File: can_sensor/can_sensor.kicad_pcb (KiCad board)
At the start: 2 copper layers, 53.3 x 25.4 mm, 54 parts, among them P1 IO1, P2 IO2, P4 CONN_01X03, P5 USB, P6 CAN_IN, P7 CAN_OUT, SW1 RESET, SW2 BOOT, U1 NJM2870F0, U2 MIC5317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

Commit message: Fixed boot button going to boot1 instead of boot0
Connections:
- P1 pad 0: GND -> (no net)
- P2 pad 0: GND -> (no net)
- P6 pad 0: GND -> (no net)
- P7 pad 0: GND -> (no net)
- U3 pad 1: Net-(U3-Pad1) -> (no net)
- U3 pad 10: Net-(U3-Pad10) -> (no net)
- U3 pad 11: Net-(U3-Pad11) -> (no net)
- U3 pad 12: Net-(U3-Pad12) -> (no net)
- U3 pad 13: Net-(U3-Pad13) -> (no net)
- U3 pad 14: Net-(U3-Pad14) -> (no net)
- U3 pad 15: Net-(U3-Pad15) -> (no net)
- U3 pad 16: Net-(U3-Pad16) -> (no net)
- U3 pad 19: Net-(U3-Pad19) -> (no net)
- U3 pad 2: Net-(U3-Pad2) -> (no net)
- U3 pad 20: Net-(R9-Pad1) -> GND
- U3 pad 21: Net-(U3-Pad21) -> (no net)
- U3 pad 22: Net-(U3-Pad22) -> (no net)
- U3 pad 25: Net-(U3-Pad25) -> (no net)
- U3 pad 26: Net-(U3-Pad26) -> (no net)
- U3 pad 27: Net-(U3-Pad27) -> (no net)
- U3 pad 28: Net-(U3-Pad28) -> (no net)
- U3 pad 29: Net-(U3-Pad29) -> (no net)
- U3 pad 3: Net-(U3-Pad3) -> (no net)
- U3 pad 30: Net-(U3-Pad30) -> (no net)
- U3 pad 31: Net-(U3-Pad31) -> (no net)
- U3 pad 38: Net-(U3-Pad38) -> (no net)
- U3 pad 4: Net-(U3-Pad4) -> (no net)
- U3 pad 41: Net-(U3-Pad41) -> (no net)
- U3 pad 42: Net-(U3-Pad42) -> (no net)
- U3 pad 43: Net-(U3-Pad43) -> (no net)
- U3 pad 44: Net-(U3-Pad44) -> Net-(R9-Pad1)
- U3 pad 5: Net-(U3-Pad5) -> (no net)
- U3 pad 6: Net-(U3-Pad6) -> (no net)
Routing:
- net Net-(R9-Pad1): track 45.5 -> 41.2 mm
- net GND: track 256.7 -> 260.4 mm

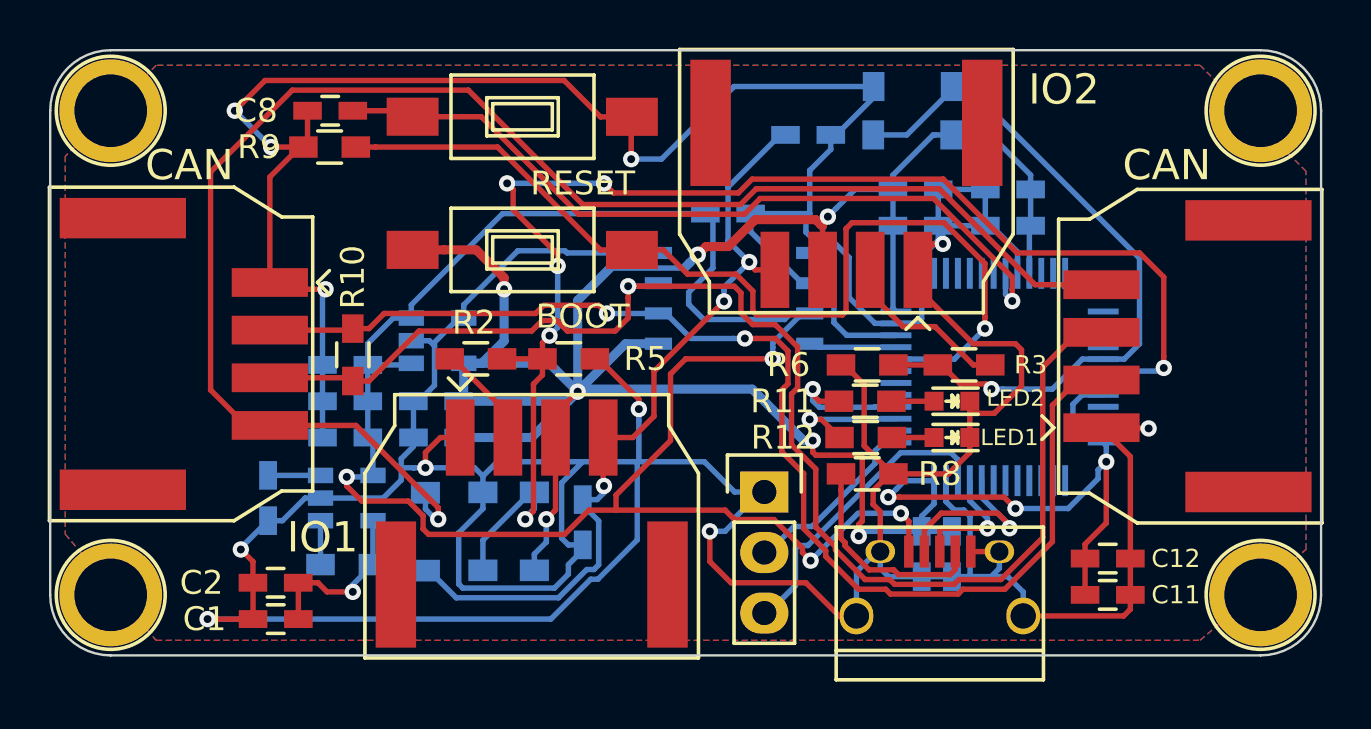
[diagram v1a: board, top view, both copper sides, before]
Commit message: revised CanSensor board to v2.0
* Jumper to enable and disable 120 Ohm termination resistor
* IO pin to mcp2562 to enable disable the CAN tranciever
* Replaced input protection diodes with a zener diode
* Replaced reverse battery protection diode with a transistor (ideal diode)
* Better silkscreen comments
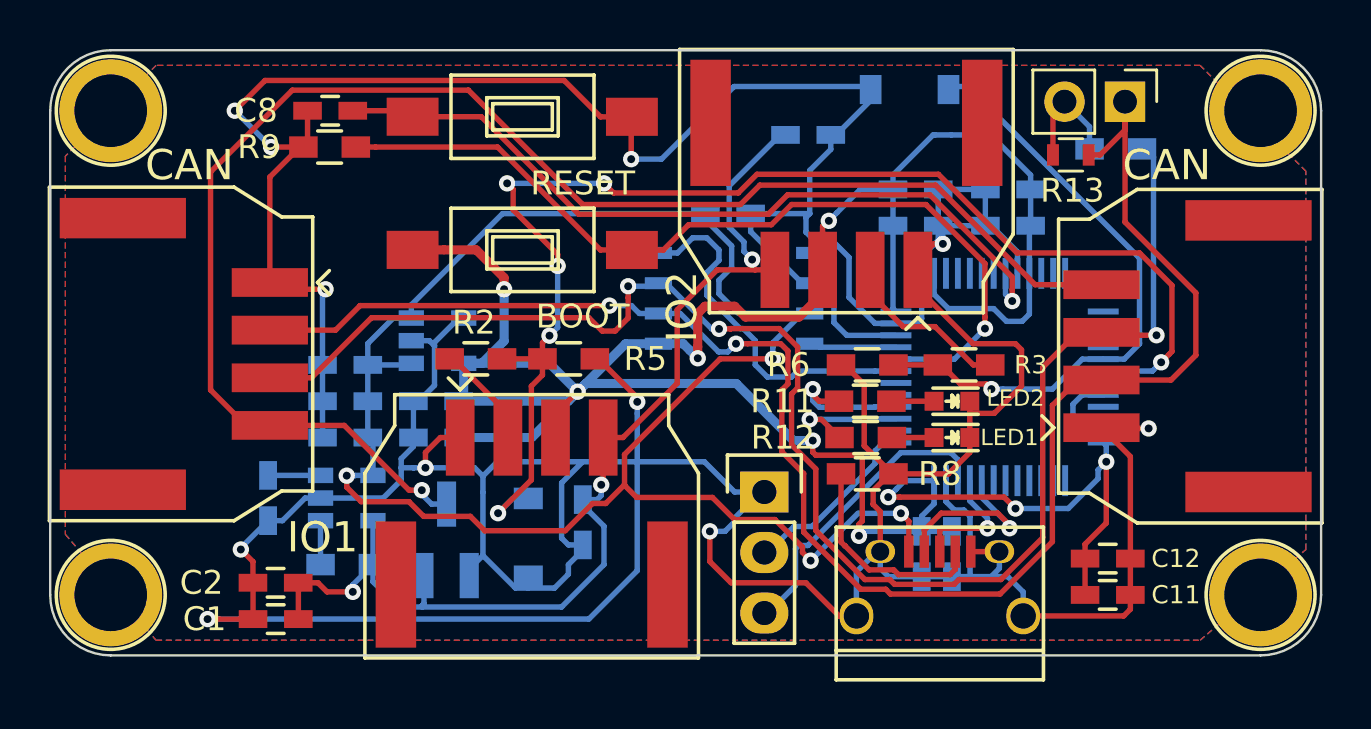
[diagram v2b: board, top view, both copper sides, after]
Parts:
- removed D3, D4: hi_v, Diodes_SMD:SOD-123
- removed D7: reverse, Diodes_SMD:SOD-123
- added P8: TERM, Pin_Headers:Pin_Header_Straight_1x02_Pitch2.54mm, F.Cu at (154.3, 96.8)
- added Q1: Q_PMOS_GSD, TO_SOT_Packages_SMD:SOT-23_Handsoldering, B.Cu at (125.9, 115.2)
- added R13: Jump, Resistors_SMD:R_0603, F.Cu at (152.1, 99.0)
- D1, D2: value hi_v -> D_Zener_Small
- R10: moved to B.Cu
- moved R10 33.2 mm to (153.9, 98.8), turned to 180 degrees
- moved D2 25.8 mm to (145.3, 96.3), turned to 180 degrees
- moved D1 0.36 mm to (129.3, 115.1), turned to 270 degrees
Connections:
- D1 pad 1: +3V3 -> /io1
- D1 pad 2: /io1 -> GND
- D2 pad 1: /io1 -> /io2
- R10 pad 2: /CAN_L -> Net-(P8-Pad2)
- U3 pad 1: (no net) -> +3V3
- U3 pad 10: (no net) -> Net-(U3-Pad10)
- U3 pad 11: (no net) -> Net-(U3-Pad11)
- U3 pad 12: (no net) -> Net-(U3-Pad12)
- U3 pad 13: (no net) -> Net-(U3-Pad13)
- U3 pad 14: (no net) -> Net-(U3-Pad14)
- U3 pad 15: (no net) -> Net-(U3-Pad15)
- U3 pad 16: (no net) -> Net-(U3-Pad16)
- U3 pad 19: (no net) -> Net-(U3-Pad19)
- U3 pad 2: (no net) -> Net-(U3-Pad2)
- U3 pad 21: (no net) -> Net-(U3-Pad21)
- U3 pad 22: (no net) -> Net-(U3-Pad22)
- U3 pad 25: (no net) -> Net-(U3-Pad25)
- U3 pad 26: (no net) -> Net-(U3-Pad26)
- U3 pad 27: (no net) -> Net-(U3-Pad27)
- U3 pad 28: (no net) -> Net-(U3-Pad28)
- U3 pad 29: (no net) -> Net-(U3-Pad29)
- U3 pad 3: (no net) -> Net-(U3-Pad3)
- U3 pad 30: (no net) -> Net-(U3-Pad30)
- U3 pad 31: (no net) -> Net-(U3-Pad31)
- U3 pad 38: (no net) -> Net-(U3-Pad38)
- U3 pad 4: (no net) -> Net-(U3-Pad4)
- U3 pad 41: (no net) -> Net-(U3-Pad41)
- U3 pad 42: (no net) -> Net-(U3-Pad42)
- U3 pad 43: (no net) -> /CAN_EN
- U3 pad 5: (no net) -> Net-(U3-Pad5)
- U3 pad 6: (no net) -> Net-(U3-Pad6)
- U4 pad 8: GND -> /CAN_EN
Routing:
- net /CAN_L: track 51.8 -> 71.4 mm
- net /CAN_EN: track 0.00 -> 15.2 mm
- net GND: track 260.4 -> 250.9 mm
- net /CAN_H: track 57.6 -> 66.4 mm, vias 1 -> 3
- net Net-(P8-Pad2): track 0.00 -> 4.85 mm
- net Net-(R9-Pad1): track 41.2 -> 37.0 mm
- net /io2: track 30.2 -> 26.2 mm
- net +3V3: track 122.9 -> 119.2 mm, vias 10 -> 9
- net /io1: track 59.0 -> 55.5 mm
- net +5V: track 78.3 -> 75.1 mm
- net VDD: track 43.0 -> 45.8 mm, vias 4 -> 3
- net /Vin: track 65.4 -> 64.0 mm
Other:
- board text added: "CanSensor 2.0"
- board text added: "IN-[R2]-+-OUT | [R5] | GND"
- board text added: "R2 (R3) and R5 (R6) attenuate input voltage"
- board text added: "Sam Ellicott - Summer 2017"
- board text removed: "Sam Ellicott - Fall 2016"
